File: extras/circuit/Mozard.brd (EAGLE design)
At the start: 94 x 71.1 mm, 44 parts, among them J4 Headphone/Line Out, U2 LM386

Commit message: Updated
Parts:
- C1: value 4.7nF -> 4.7nF/472
- C2: value 10uF -> 10uF/106
- C4: value 100nF -> 100nF/104
- moved R1 18.7 mm to (71.1, 36.2)
- moved R2 18.7 mm to (71.1, 33.7)
- moved U2 0.90 mm to (42.5, 52.7)
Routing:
- net N$3: track 32.1 -> 58.3 mm
- net TX: track 53.6 -> 34.0 mm
- net N$5: track 29.0 -> 44.1 mm
- net A1: track 83.4 -> 96.9 mm, vias 1 -> 0
- net VCC: track 125.9 -> 116.4 mm, vias 2 -> 1
- net V+: track 44.6 -> 52.9 mm
- net GND: track 313.3 -> 315.5 mm
- net N$7: track 9.92 -> 10.8 mm
- net RX: track 43.4 -> 44.1 mm
- added copper zone on layer 1, net GND
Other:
- board text added: "MOZARD 2018-09-25 TOFSTUFF.COM"
- board text removed: "MOZARD 2018-08-01 TOFFSTUFF.COM"
- board text removed: "TODO: - make 499k larger"

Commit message: Update extras/circuit/Mozard.brd
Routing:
- net D3: track 78.3 -> 79.4 mm
- net D7: track 72.8 -> 73.6 mm
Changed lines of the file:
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@@
 <contactref element="U$1" pad="D3"/>
 <contactref element="TOUCH14" pad="1"/>
-<wire x1="74.688721875" y1="18.021278125" x2="67.31" y2="25.4" width="0.254" layer="1"/>
-<wire x1="74.794675" y1="18.021278125" x2="74.688721875" y2="18.021278125" width="0.254" layer="1"/>
-<wire x1="77.47" y1="15.345953125" x2="74.794675" y2="18.021278125" width="0.254" layer="1"/>
-<wire x1="77.47" y1="10.16" x2="77.47" y2="15.345953125" width="0.254" layer="1"/>
-<wire x1="67.31" y1="25.4" x2="36.195" y2="25.4" width="0.254" layer="1"/>
+<wire x1="69.608721875" y1="25.006278125" x2="69.215" y2="25.4" width="0.254" layer="1"/>
+<wire x1="69.714675" y1="25.006278125" x2="69.608721875" y2="25.006278125" width="0.254" layer="1"/>
+<wire x1="77.47" y1="17.250953125" x2="69.714675" y2="25.006278125" width="0.254" layer="1"/>
+<wire x1="77.47" y1="10.16" x2="77.47" y2="17.250953125" width="0.254" layer="1"/>
+<wire x1="69.215" y1="25.4" x2="36.195" y2="25.4" width="0.254" layer="1"/>
 <wire x1="36.195" y1="25.4" x2="27.94" y2="33.655" width="0.254" layer="1"/>
 <wire x1="27.94" y1="33.655" x2="27.94" y2="42.545" width="0.254" layer="1"/>
@@
 <contactref element="TOUCH10" pad="1"/>
 <contactref element="U$1" pad="D7"/>
-<wire x1="57.15" y1="10.16" x2="57.15" y2="15.875" width="0.254" layer="1"/>
-<wire x1="57.15" y1="15.875" x2="52.07" y2="20.955" width="0.254" layer="1"/>
-<wire x1="52.07" y1="20.955" x2="35.56" y2="20.955" width="0.254" layer="1"/>
+<wire x1="57.15" y1="10.16" x2="57.15" y2="17.145" width="0.254" layer="1"/>
+<wire x1="57.15" y1="17.145" x2="53.34" y2="20.955" width="0.254" layer="1"/>
+<wire x1="53.34" y1="20.955" x2="35.56" y2="20.955" width="0.254" layer="1"/>
 <wire x1="35.56" y1="20.955" x2="25.4" y2="31.115" width="0.254" layer="1"/>
 <wire x1="25.4" y1="31.115" x2="25.4" y2="48.895" width="0.254" layer="1"/>

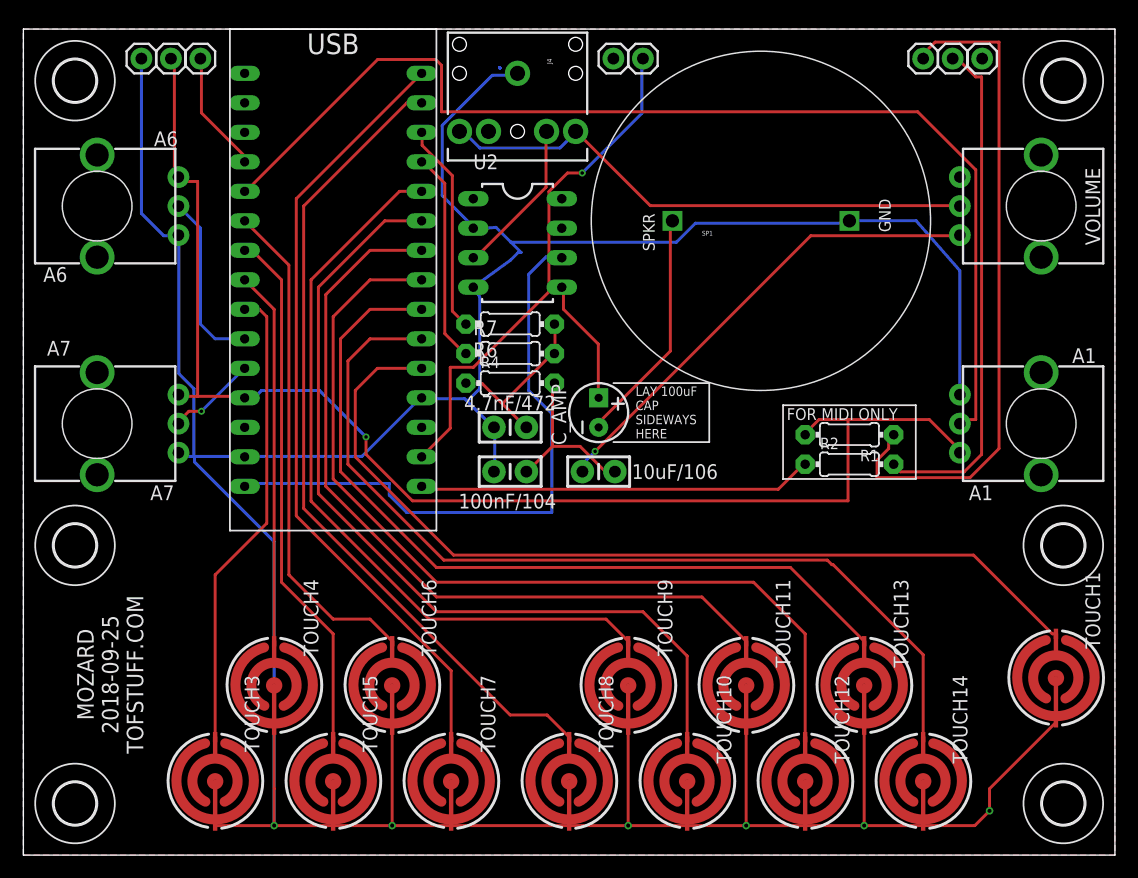
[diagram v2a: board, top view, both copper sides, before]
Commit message: Fixed overlapping traces
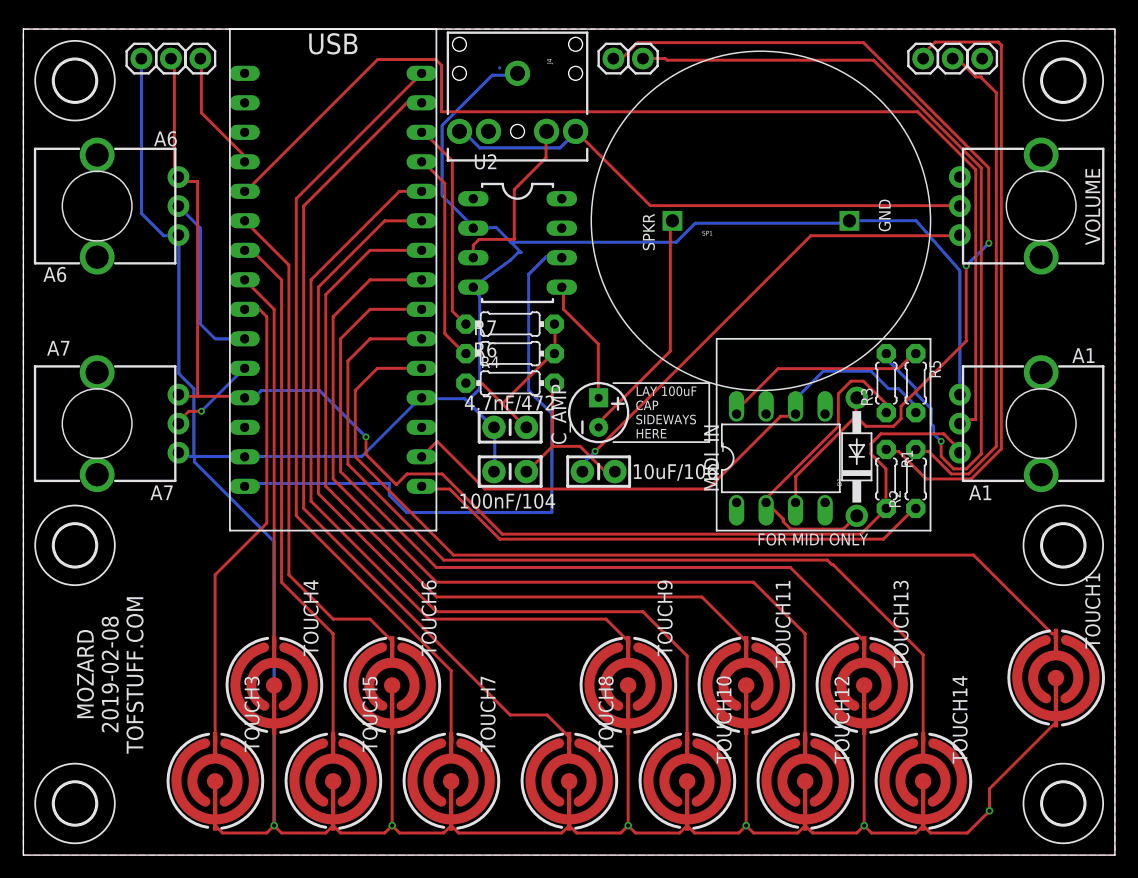
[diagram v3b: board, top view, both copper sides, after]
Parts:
- added D1: 1N4148, adafruit:DO41-10
- added MIDI_IN: 6N138, optocoupler:DIL08
- added R3: 220, adafruit:0204/5
- added R5: 270, adafruit:0204/5
- JP1: value MIDI 5V -> MIDITX4
- JP4: value GND -> MIDIRX5
- MIDI_TX: value MIDI TX -> MIDITX5
- R1, R2: device adafruit:0204/7 -> adafruit:0204/5
- RX: value RX -> MIDIRX4
- moved R2 5.85 mm to (76.8, 32.4), turned to 90 degrees
- moved R1 4.96 mm to (74.3, 32.4), turned to 270 degrees
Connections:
- new net 5V: MIDI_IN.8, R5.1
- new net N$10: D1.C, MIDI_IN.2, R3.1
- new net N$8: D1.A, JP4.1, MIDI_IN.3
- new net N$9: R3.2, RX.1
- net GND: now also MIDI_IN.5; no longer JP4.1
- net RX: now also MIDI_IN.6, R5.2; no longer RX.1
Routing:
- net N$8: track 0.00 -> 77.8 mm, vias 0 -> 2
- net N$9: track 0.00 -> 73.0 mm, vias 0 -> 1
- net N$10: track 0.00 -> 27.4 mm
- net 5V: track 0.00 -> 17.8 mm
- net TX: track 34.0 -> 45.5 mm
- net RX: track 44.1 -> 51.6 mm, vias 1 -> 0
- net GND: track 315.5 -> 321.8 mm
- net N$3: track 58.3 -> 54.4 mm
- net N$6: track 13.6 -> 15.2 mm
- net VCC: track 116.4 -> 115.3 mm
- net _GND: track 0.59 -> 0.02 mm
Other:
- board text added: "MOZARD 2019-02-08 TOFSTUFF.COM"
- board text removed: "MOZARD 2018-09-25 TOFSTUFF.COM"

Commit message: Sensitivity change
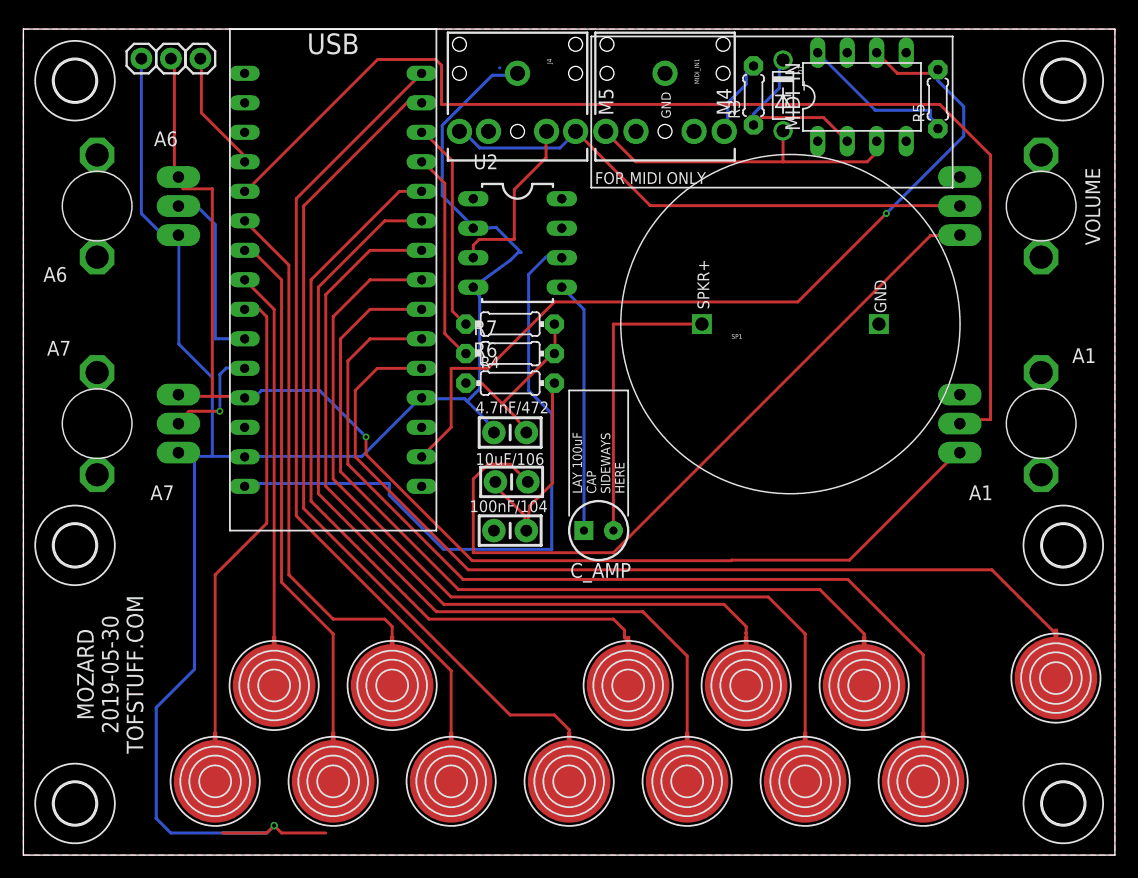
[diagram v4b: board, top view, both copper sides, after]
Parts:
- removed JP1: MIDITX4, TOF:1X01_SIDE_NAME
- removed JP3: GND, TOF:1X01_SIDE_NAME
- removed JP4: MIDIRX5, TOF:1X01_SIDE_NAME
- removed MIDI_TX: MIDITX5, TOF:1X01_SIDE_NAME
- removed R1, R2: 220, adafruit:0204/5
- removed RX: MIDIRX4, TOF:1X01_SIDE_NAME
- removed TOUCH1, TOUCH10, TOUCH11, TOUCH12, TOUCH13, TOUCH14, TOUCH3, TOUCH4, TOUCH5, TOUCH6, TOUCH7, TOUCH8, TOUCH9: (no value), TOF:PCB-TOUCHPAD2
- added MIDI_IN1: AUDIO-JACKKIT, TOF:AUDIO-JACK-KIT
- added U$10, U$11, U$12, U$13, U$14, U$2, U$3, U$4, U$5, U$6, U$7, U$8, U$9: PCB-TOUCHPAD-1-PIN, TOF:PCB-TOUCHPAD-1-PIN
- A1, A6, A7, VOLUME: device SparkFun-Electromechanical:ALPS_POT_KIT -> TOF:ALPS_POT
- D1: device adafruit:DO41-10 -> TOF:DO41-10
- MIDI_IN: device optocoupler:DIL08 -> TOF:DIL08
- moved MIDI_IN 31.9 mm to (72.2, 65.3)
- moved D1 31.8 mm to (65.4, 65.4), turned to 270 degrees
- moved R3 27.3 mm to (62.9, 65.4)
- moved R5 24.5 mm to (78.7, 65.1), turned to 90 degrees
- moved C_AMP 10.2 mm to (49.5, 27.9), turned to 180 degrees
- moved SP1 9.25 mm to (66.0, 45.7)
- moved C2 7.55 mm to (42.0, 32.1), turned to 0 degrees
- moved C4 5.08 mm to (41.9, 27.9)
- moved C1 0.44 mm to (41.9, 36.4)
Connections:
- removed net N$3: JP1.1, R1.1
- removed net N$5: MIDI_TX.1, R2.2
- removed net N$8: D1.A, JP4.1, MIDI_IN.3
- removed net N$9: R3.2, RX.1
- new net M4: MIDI_IN1.RING, R3.2
- new net M5: D1.A, MIDI_IN.3, MIDI_IN1.TIP
- net A2: now also U$5.1; no longer TOUCH6.1
- net A3: now also U$4.1; no longer TOUCH5.1
- net A4: now also U$3.1; no longer TOUCH4.1
- net A5: now also U$2.1; no longer TOUCH3.1
- net D11: now also U$7.1; no longer TOUCH8.1
- net D12: now also U$6.1; no longer TOUCH7.1
- net D3: now also U$13.1; no longer TOUCH14.1
- net D4: now also U$12.1; no longer TOUCH13.1
- net D5: now also U$11.1; no longer TOUCH12.1
- net D6: now also U$10.1; no longer TOUCH11.1
- net D7: now also U$9.1; no longer TOUCH10.1
- net D8: now also U$8.1; no longer TOUCH9.1
- net GND: now also MIDI_IN1.SLEEVE; no longer JP3.1, TOUCH1.2, TOUCH10.2, TOUCH11.2, TOUCH12.2, TOUCH13.2, TOUCH14.2, TOUCH3.2, TOUCH4.2, TOUCH5.2, TOUCH6.2, TOUCH7.2, TOUCH8.2, TOUCH9.2
- net TOUCH_A: now also U$14.1; no longer TOUCH1.1
- net TX: no longer R2.1
- net VCC: no longer R1.2
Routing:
- net GND: track 321.8 -> 160.3 mm, vias 6 -> 1
- net N$8: track 77.8 -> 0.00 mm, vias 2 -> 0
- net N$9: track 73.0 -> 0.00 mm, vias 1 -> 0
- net N$3: track 54.4 -> 0.00 mm
- net TX: track 45.5 -> 0.00 mm
- net N$5: track 44.3 -> 0.00 mm
- net M5: track 0.00 -> 28.4 mm
- net N$2: track 41.3 -> 65.4 mm, vias 1 -> 0
- net RX: track 51.6 -> 73.9 mm, vias 0 -> 1
- net N$10: track 27.4 -> 15.8 mm
- net N$7: track 10.8 -> 21.7 mm
- net M4: track 0.00 -> 6.70 mm
- net N$1: track 20.4 -> 25.4 mm
- net V+: track 52.9 -> 57.4 mm
- net VCC: track 115.3 -> 110.9 mm
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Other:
- board text added: "M4"
- board text added: "M5"
- board text added: "MOZARD 2019-05-30 TOFSTUFF.COM"
- board text added: "SPKR+"
- board text removed: "MOZARD 2019-02-08 TOFSTUFF.COM"
- board text removed: "SPKR"
